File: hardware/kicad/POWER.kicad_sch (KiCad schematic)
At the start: 7 parts, among them J1 Conn_01x02_Pin

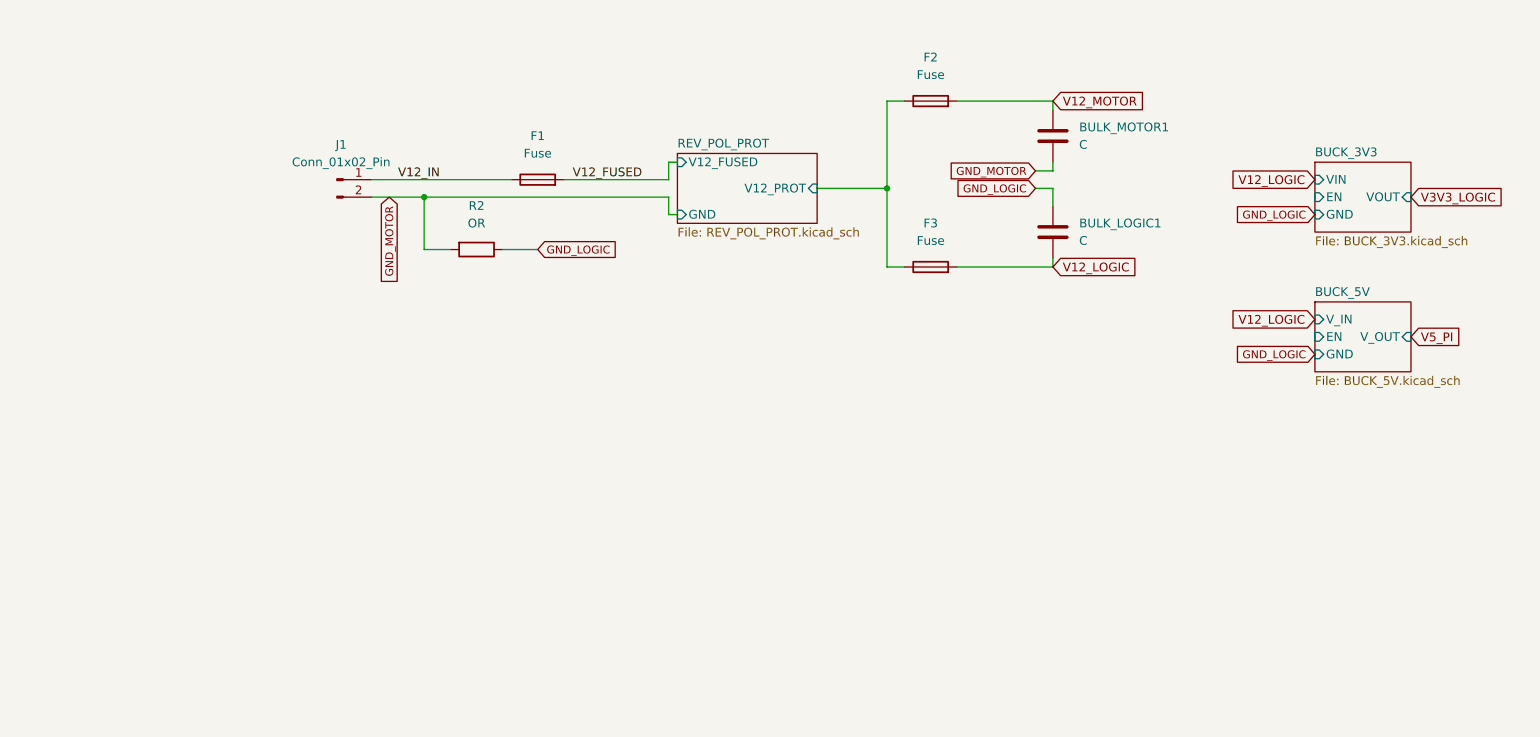
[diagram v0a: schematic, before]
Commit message: feat: buck 12-3.3V schematic structure complete
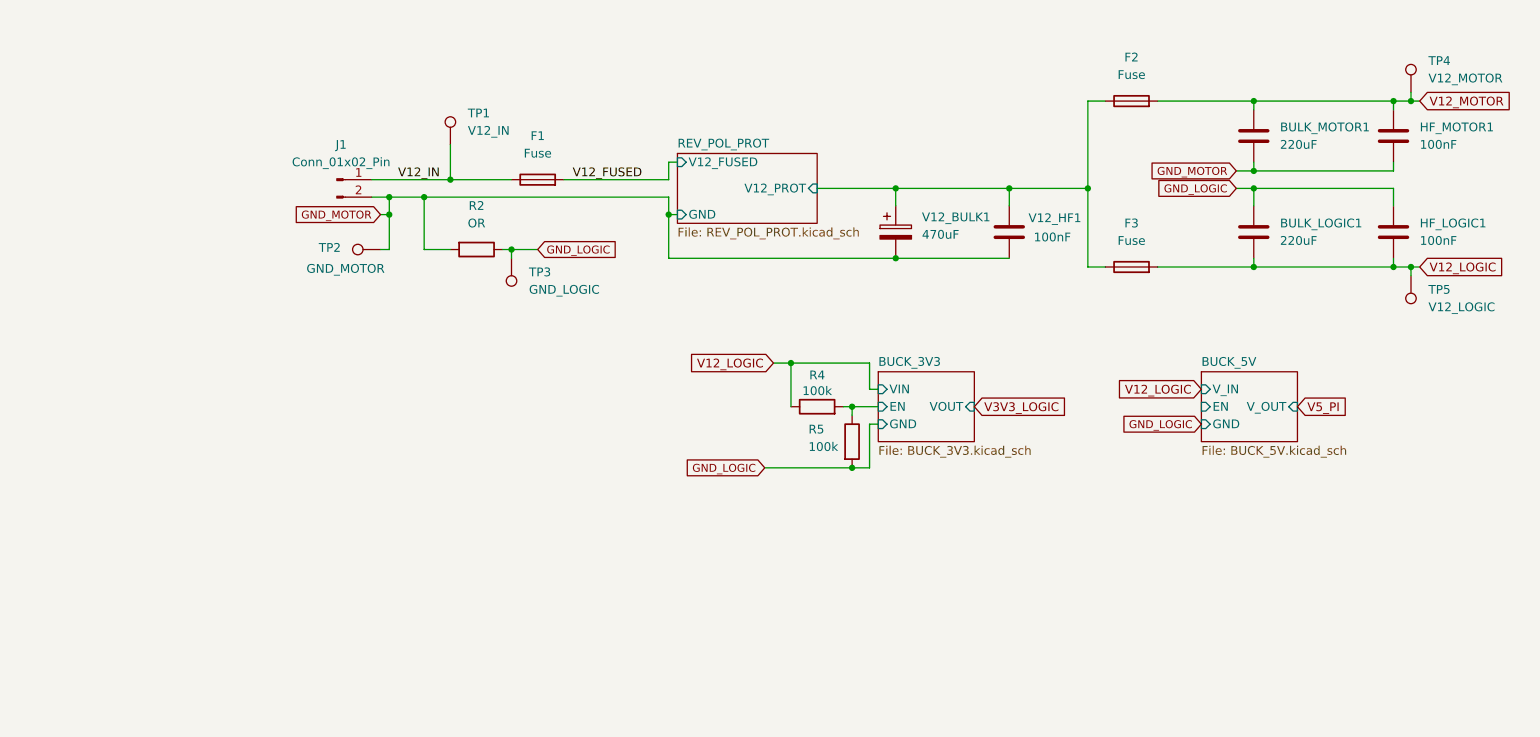
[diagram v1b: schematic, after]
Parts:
- added HF_LOGIC1, HF_MOTOR1, V12_HF1: 100nF, symbol Device:C
- added R4: 100k, Resistor_SMD:R_1206_3216Metric_Pad1.30x1.75mm_HandSolder, symbol Device:R
- added R5: 100k, symbol Device:R
- added TP1: V12_IN, symbol Connector:TestPoint
- added TP2: GND_MOTOR, symbol Connector:TestPoint
- added TP3: GND_LOGIC, symbol Connector:TestPoint
- added TP4: V12_MOTOR, symbol Connector:TestPoint
- added TP5: V12_LOGIC, symbol Connector:TestPoint
- added V12_BULK1: 470uF, symbol Device:C_Polarized
- BULK_LOGIC1, BULK_MOTOR1: value C -> 220uF
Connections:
- net BUCK_3V3/EN: now also R4.2, R5.1
- net GND_LOGIC: now also HF_LOGIC1.1, R5.2, TP3.1
- net GND_MOTOR: now also HF_MOTOR1.2, TP2.1, V12_BULK1.2, V12_HF1.2
- net REV_POL_PROT/V12_PROT: now also V12_BULK1.1, V12_HF1.1
- net V12_IN: now also TP1.1
- net V12_LOGIC: now also HF_LOGIC1.2, R4.1, TP5.1
- net V12_MOTOR: now also HF_MOTOR1.1, TP4.1
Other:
- moved on the sheet: BULK_LOGIC1, BULK_MOTOR1, F2, F3

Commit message: fix: changed to TPSM82903 - PG not connected yet
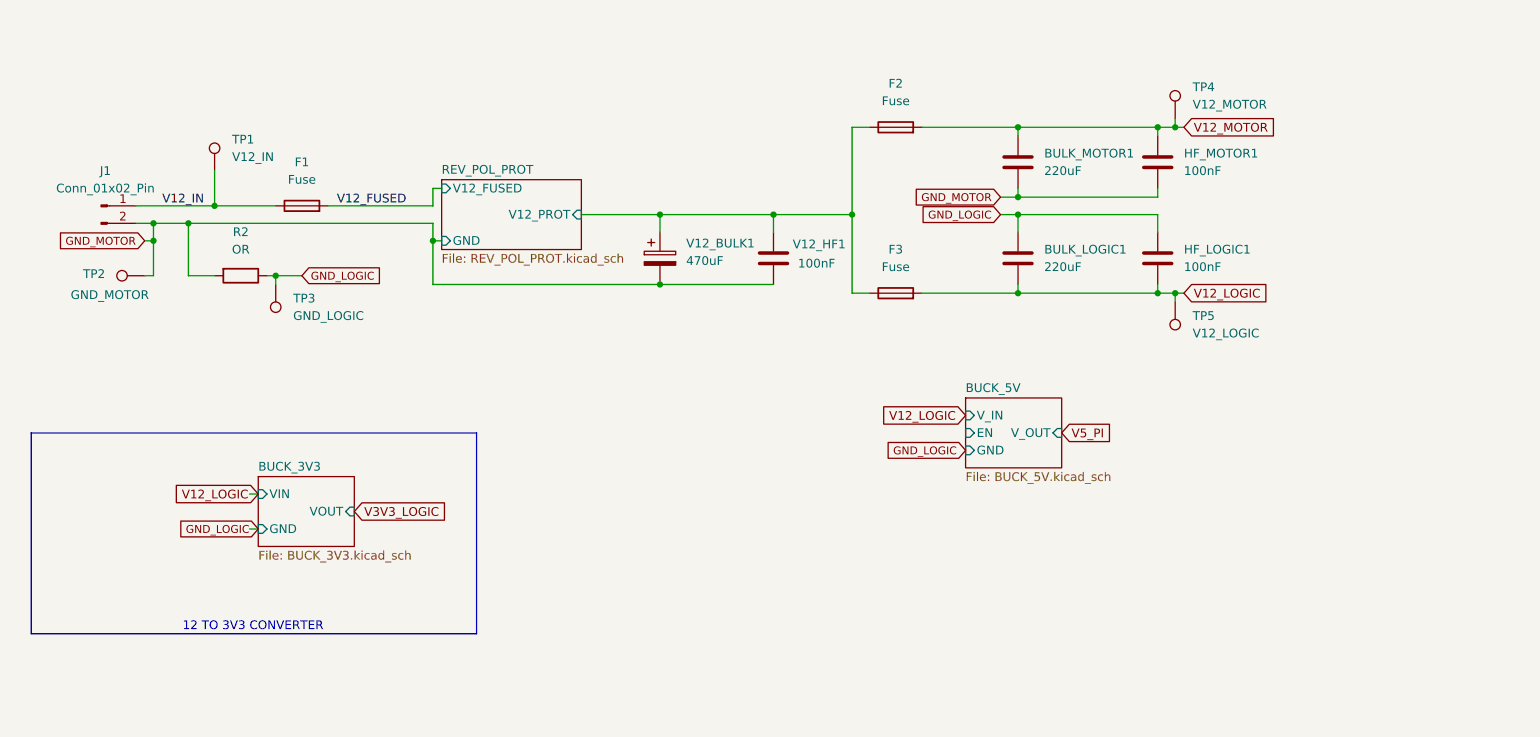
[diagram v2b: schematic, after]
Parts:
- removed R4: 100k, Resistor_SMD:R_1206_3216Metric_Pad1.30x1.75mm_HandSolder, symbol Device:R
- removed R5: 100k, symbol Device:R
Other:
- sheet BUCK_3V3 ports: added none; removed EN
- note added: "12 TO 3V3 CONVERTER"
- moved on the sheet: BULK_LOGIC1, BULK_MOTOR1, F1, F2, F3, HF_LOGIC1, HF_MOTOR1, J1, R2, TP1, TP2, TP3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

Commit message: feat: implemented keypad & reverse polarity protection
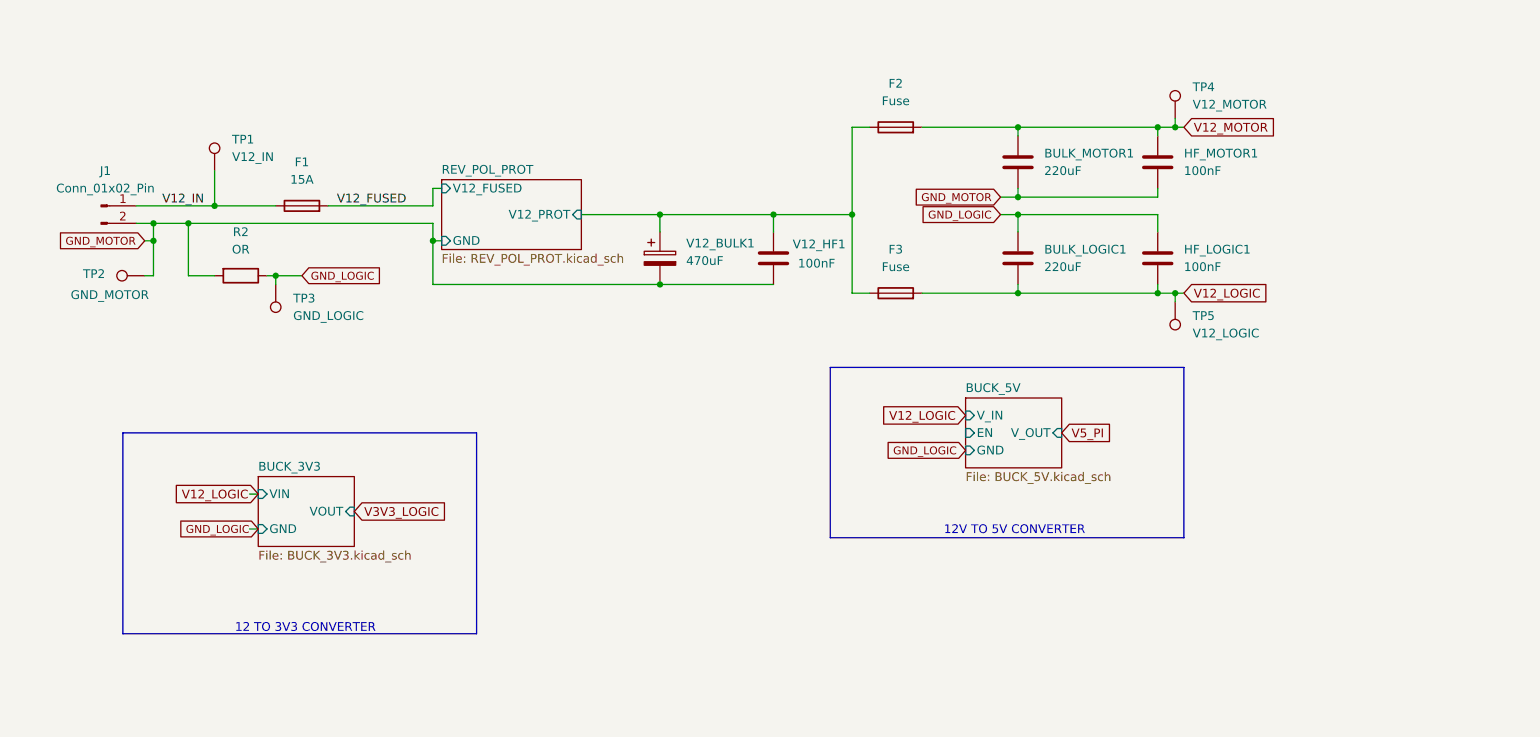
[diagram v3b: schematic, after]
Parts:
- F1: value Fuse -> 15A
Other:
- note added: "12V TO 5V CONVERTER"
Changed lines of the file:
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@@
 	(paper "A4")
 	(rectangle
-		(start 54.61 104.14)
+		(start 67.945 104.14)
 		(end 119.38 133.35)
 		(stroke
@@
 		)
 	)
+	(rectangle
+		(start 170.815 94.615)
+		(end 222.25 119.38)
+		(stroke
+			(width 0)
+			(type default)
+		)
+		(fill
+			(type none)
+		)
+	)
+	(text "12V TO 5V CONVERTER\n"
+		(exclude_from_sim no)
+		(at 197.612 118.364 0)
+		(effects
+			(font
+				(size 1.27 1.27)
+			)
+		)
+	)
 	(text "12 TO 3V3 CONVERTER\n"
 		(exclude_from_sim no)
-		(at 86.868 132.334 0)
+		(at 94.488 132.588 0)
 		(effects
 			(font
@@
 			)
 		)
-		(property "Value" "Fuse"
+		(property "Value" "15A"
 			(at 93.98 67.31 90)
 			(effects

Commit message: fix: error fixing & connection config
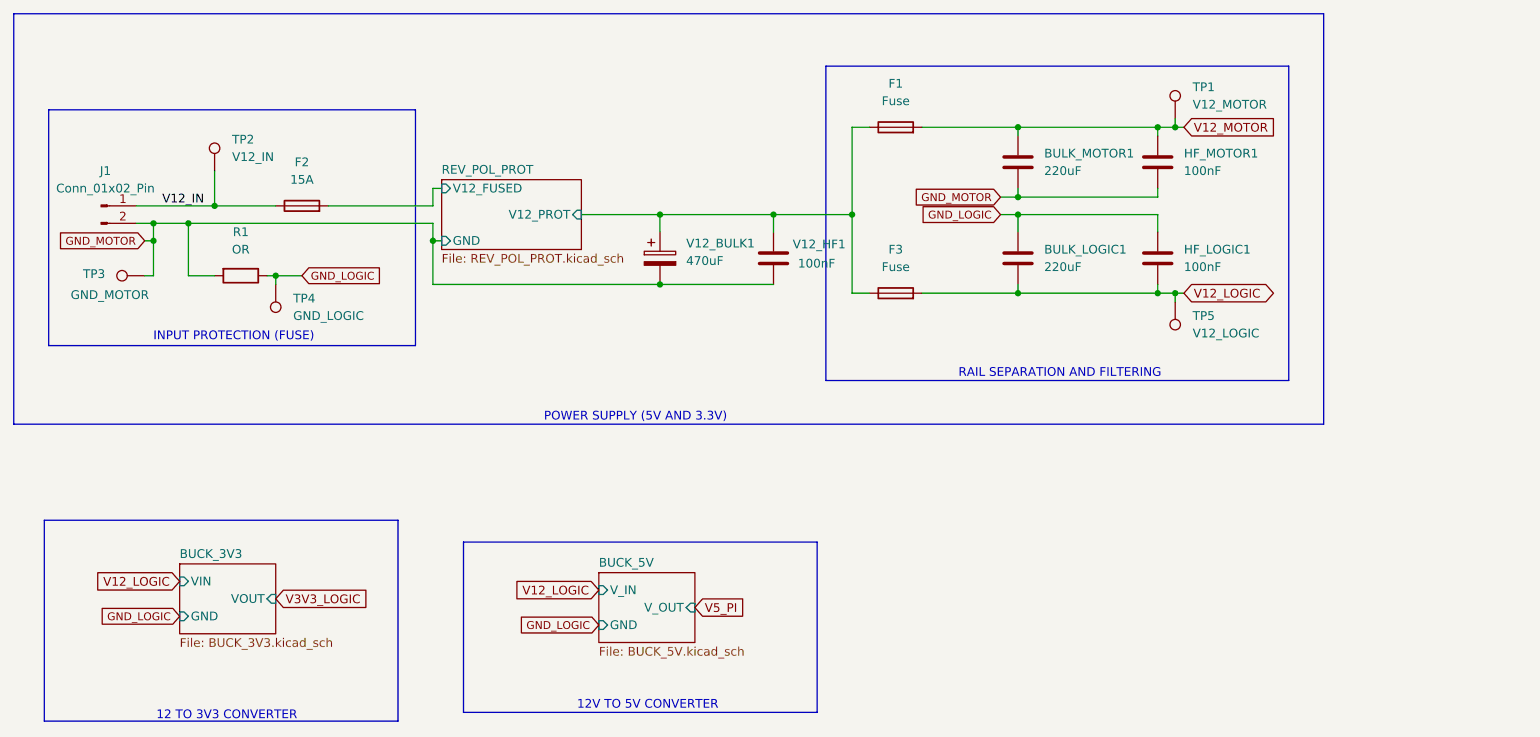
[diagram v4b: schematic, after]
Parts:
- renumbered F2 to F1, F1 to F2, R2 to R1, TP4 to TP1, TP1 to TP2, TP2 to TP3, TP3 to TP4
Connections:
- net V12_FUSED renamed REV_POL_PROT/V12_FUSED
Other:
- sheet BUCK_5V ports: added none; removed EN
- note added: "INPUT PROTECTION (FUSE)"
- note added: "POWER SUPPLY (5V AND 3.3V)"
- note added: "RAIL SEPARATION AND FILTERING"

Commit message: docs: added end semester report for project
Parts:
- BULK_LOGIC1, BULK_MOTOR1, HF_LOGIC1, HF_MOTOR1, V12_HF1: symbol Device:C -> TPSM82903:C
- F1, F2, F3: symbol Device:Fuse -> TPSM82903:Fuse
- J1: symbol Connector:Conn_01x02_Pin -> TPSM82903:Conn_01x02_Pin
- R1: symbol Device:R -> TPSM82903:R
- TP1, TP2, TP3, TP4, TP5: symbol Connector:TestPoint -> TPSM82903:TestPoint
- V12_BULK1: symbol Device:C_Polarized -> TPSM82903:C_Polarized
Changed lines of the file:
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@@
 	)
 	(symbol
-		(lib_id "Device:Fuse")
+		(lib_id "TPSM82903:Fuse")
 		(at 93.98 71.12 90)
 		(unit 1)
@@
 	)
 	(symbol
-		(lib_id "Device:C")
+		(lib_id "TPSM82903:C")
 		(at 218.44 78.74 0)
 		(unit 1)
@@
 	)
 	(symbol
-		(lib_id "Connector:TestPoint")
+		(lib_id "TPSM82903:TestPoint")
 		(at 220.98 58.42 0)
 		(unit 1)
@@
 	)
 	(symbol
-		(lib_id "Device:Fuse")
+		(lib_id "TPSM82903:Fuse")
 		(at 180.34 59.69 90)
 		(unit 1)
@@
 	)
 	(symbol
-		(lib_id "Device:C")
+		(lib_id "TPSM82903:C")
 		(at 218.44 64.77 0)
 		(unit 1)
@@
 	)
 	(symbol
-		(lib_id "Connector:TestPoint")
+		(lib_id "TPSM82903:TestPoint")
 		(at 71.12 81.28 90)
 		(unit 1)
@@
 	)
 	(symbol
-		(lib_id "Device:Fuse")
+		(lib_id "TPSM82903:Fuse")
 		(at 180.34 83.82 90)
 		(unit 1)
@@
 	)
 	(symbol
-		(lib_id "Device:R")
+		(lib_id "TPSM82903:R")
 		(at 85.09 81.28 270)
 		(unit 1)
@@
 	)
 	(symbol
-		(lib_id "Device:C")
+		(lib_id "TPSM82903:C")
 		(at 198.12 78.74 0)
 		(unit 1)
@@
 	)
 	(symbol
-		(lib_id "Device:C")
+		(lib_id "TPSM82903:C")
 		(at 198.12 64.77 0)
 		(unit 1)
@@
 	)
 	(symbol
-		(lib_id "Device:C")
+		(lib_id "TPSM82903:C")
 		(at 162.56 78.74 0)
 		(unit 1)
@@
 	)
 	(symbol
-		(lib_id "Connector:Conn_01x02_Pin")
+		(lib_id "TPSM82903:Conn_01x02_Pin")
 		(at 64.77 71.12 0)
 		(unit 1)
@@
 	)
 	(symbol
-		(lib_id "Connector:TestPoint")
+		(lib_id "TPSM82903:TestPoint")
 		(at 220.98 85.09 180)
 		(unit 1)
@@
 	)
 	(symbol
-		(lib_id "Connector:TestPoint")
+		(lib_id "TPSM82903:TestPoint")
 		(at 90.17 82.55 180)
 		(unit 1)
@@
 	)
 	(symbol
-		(lib_id "Connector:TestPoint")
+		(lib_id "TPSM82903:TestPoint")
 		(at 81.28 66.04 0)
 		(unit 1)
@@
 	)
 	(symbol
-		(lib_id "Device:C_Polarized")
+		(lib_id "TPSM82903:C_Polarized")
 		(at 146.05 78.74 0)
 		(unit 1)
